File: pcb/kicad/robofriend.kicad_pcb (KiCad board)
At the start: 2 copper layers, 92.1 x 94 mm, 122 parts, among them J1 UART, J10 12V-Buck, J11 12V-Buck-Boost, J12 5VIN, J13 5VOUT, J14 5VOUT, J15 US2, J16 US3, J17 USB_A_4_PIN, J18 12V-Reg, J19 MON/AMP, J2 VBAT, J20 US4, J21 MRi, J22 SPI, J23 MLe, J24 3V3OUT, J25 3V3OUT, J26 M1, J27 M2, J28 IR1, J29 ADC1, J3 PWR, J30 IR2, J31 ADC2, J32 IR3, J33 GS2, J4 GS2, J5 I2C, J6 I2C, J7 I2C, J8 I2C, J9 US1, K1 SCHRACK-RTx3, Q1 NMOS, Q2 NPN, Q3 PMOS, U1 74LVC1T45, U10 TL331, U2 Teensy++2.0, U3 TL331, U4 74LVC1T45, U5 PCA9517, U6 MCP6001, U7 LM3940-3.3, U8 LM4040, U9 INA193

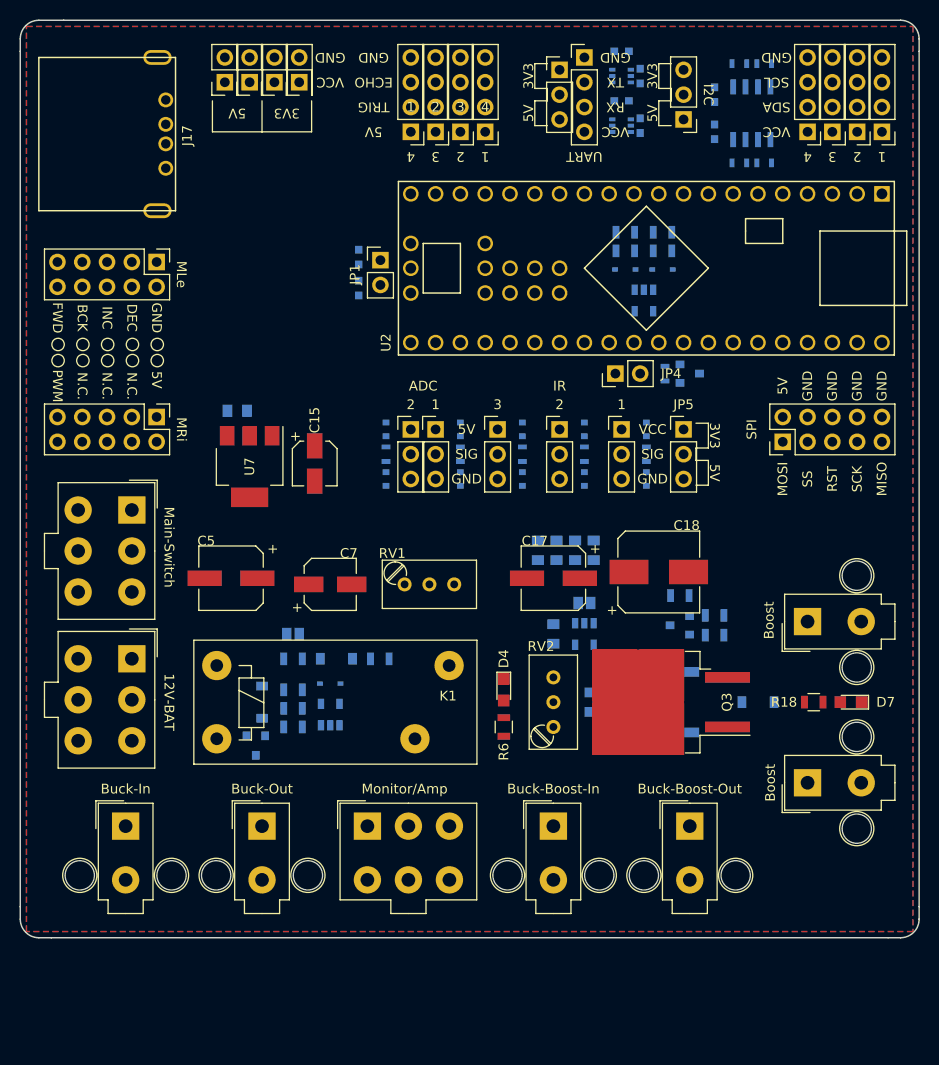
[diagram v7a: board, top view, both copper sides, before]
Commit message: completed first version of bom, minor correction in schematic and layout adoptation, new plots available
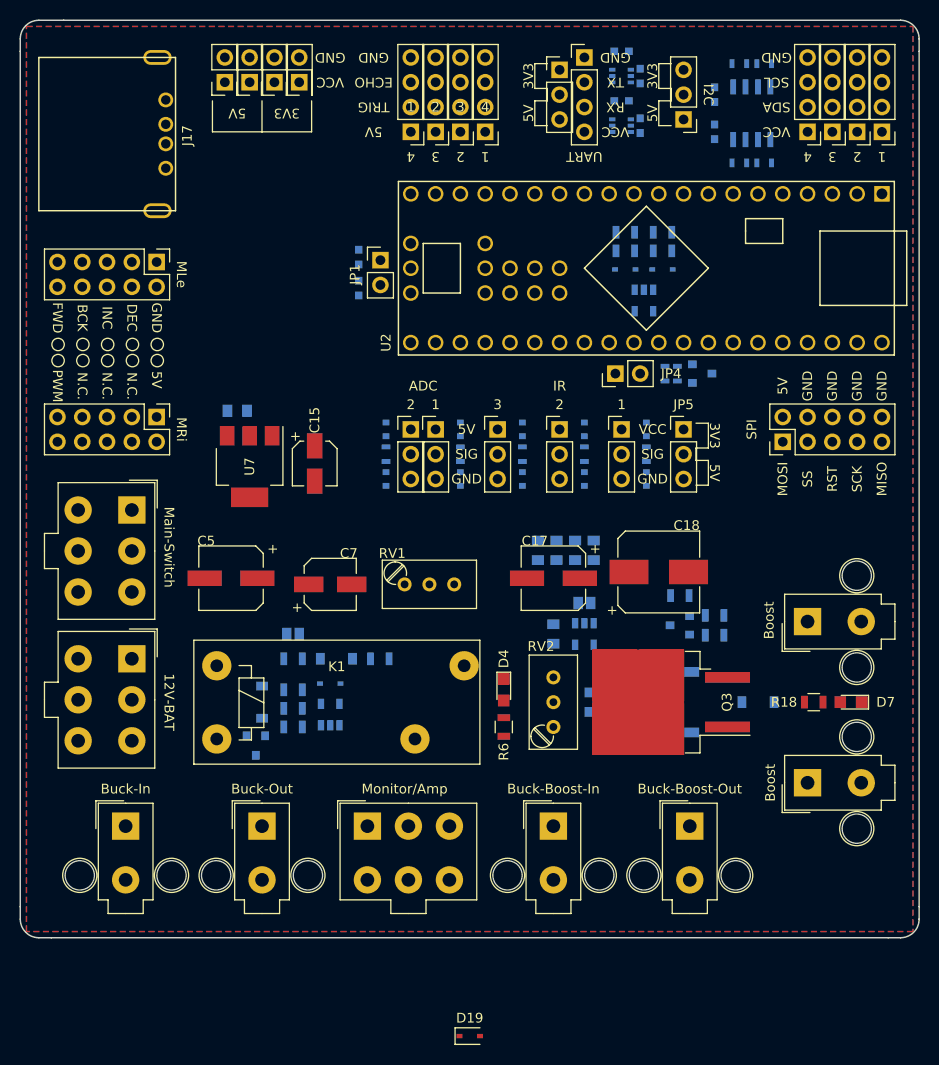
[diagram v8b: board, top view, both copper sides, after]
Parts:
- added D19: D, Diodes_SMD:D_SOD-323, F.Cu at (126.7, 171.4)
- added R28: 10k, Resistors_SMD:R_0603, B.Cu at (148.0, 103.5)
- K1: footprint Relay:SPST_Schrack-RTx3_RM3.5mm -> Relay:SPST_Schrack-RTx3_RM5mm
- moved U8 1.27 mm to (150.5, 103.5)
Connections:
- Q1 pad 3: GND -> Net-(D19-Pad2)
